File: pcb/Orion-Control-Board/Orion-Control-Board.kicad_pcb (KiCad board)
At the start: 2 copper layers, 35 x 35 mm, 36 parts, among them J1 CORTEX_DEBUG_SWD_UART, J2 STLINK_SWD_JTAG_20POS, J3 USB C 2.0 Female, U1 FT232RL, U2 USBLC6-2SC6, U3 LM66100, U4 LM66100

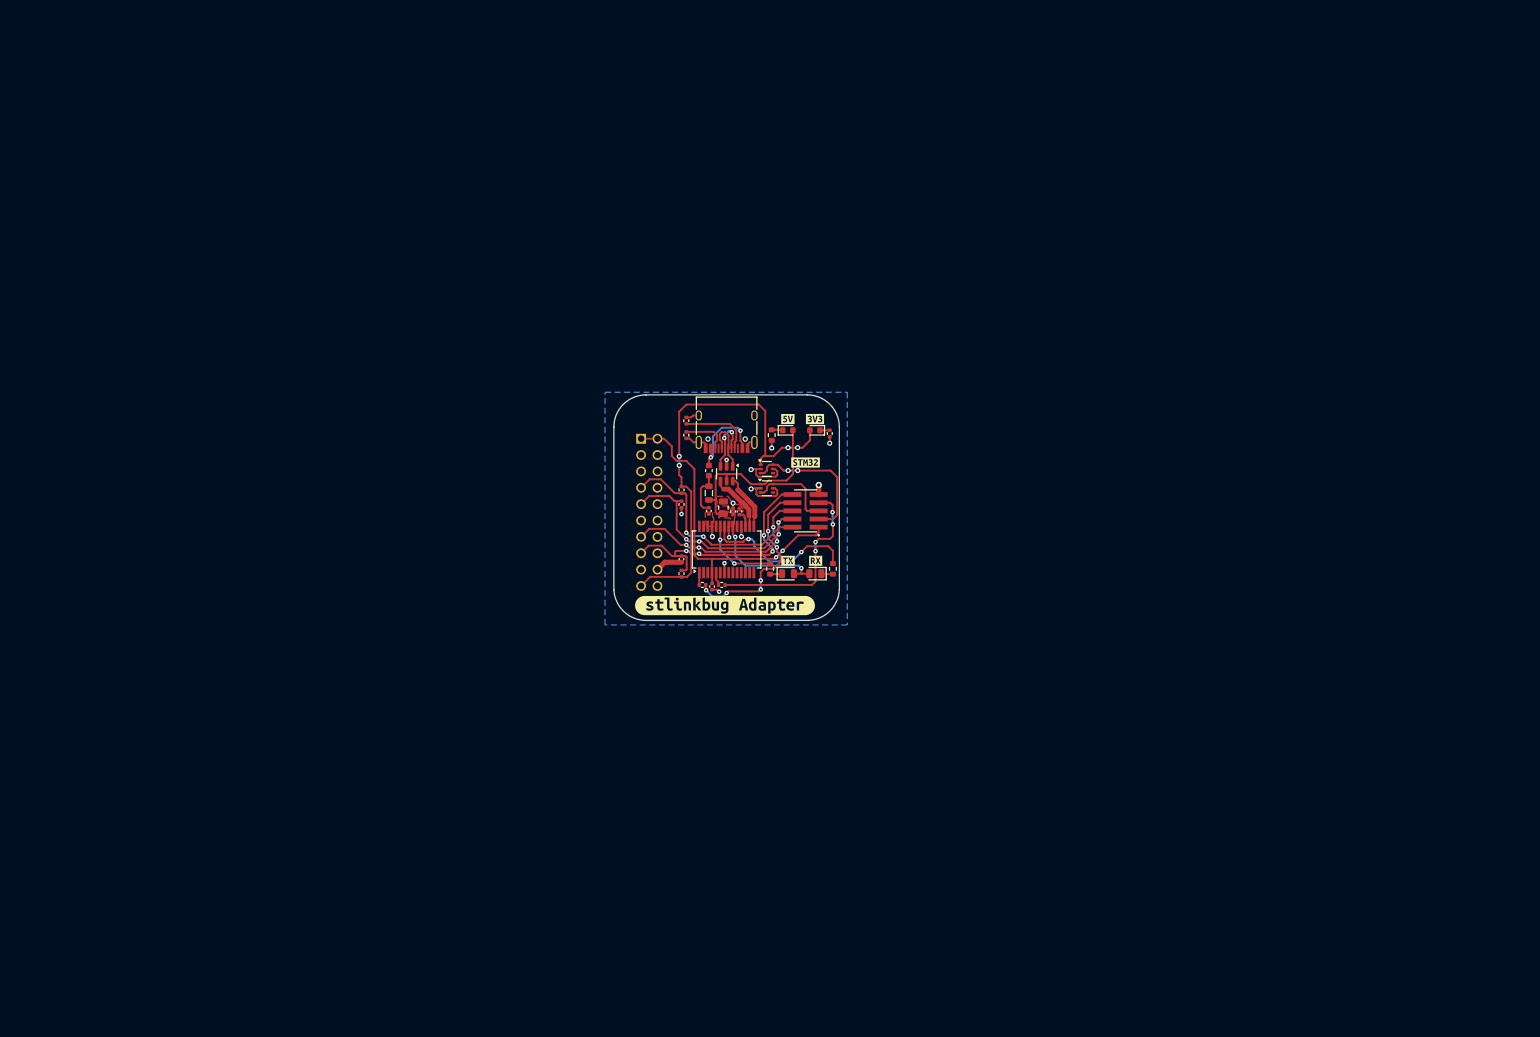
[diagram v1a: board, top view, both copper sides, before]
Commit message: Complete Schematic - Add STM32
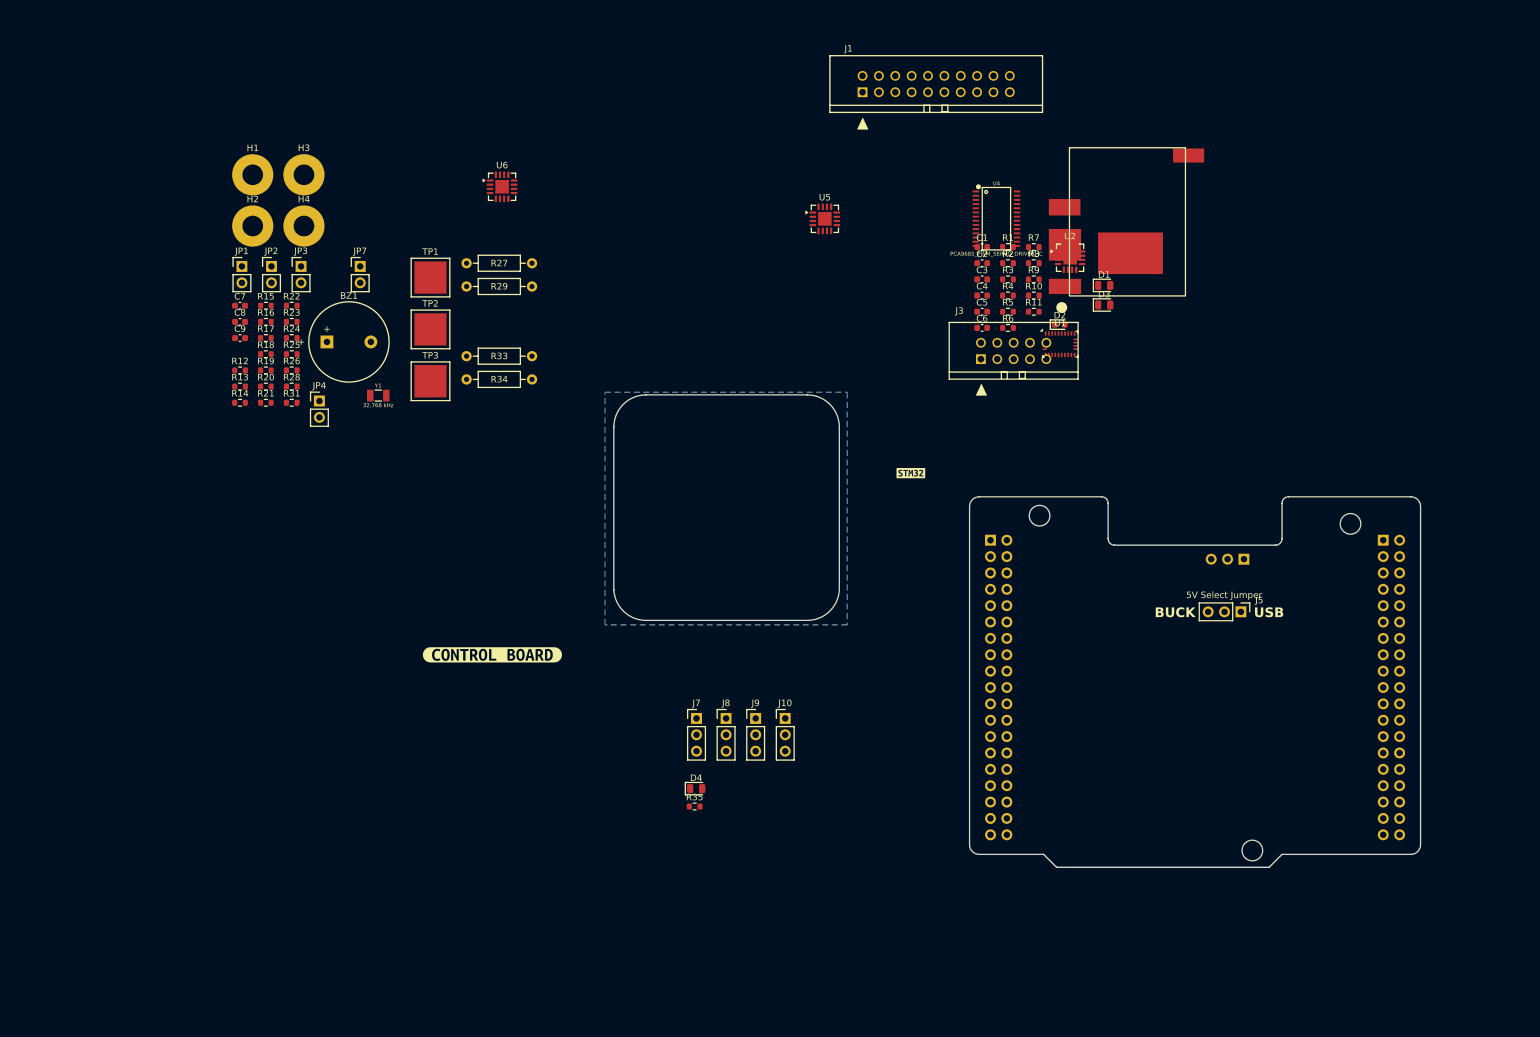
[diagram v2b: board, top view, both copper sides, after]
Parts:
- removed F1: 6V 500mA Fuse, Fuse:Fuse_0603_1608Metric
- removed FB1: 100Ω@100MHz, Inductor_SMD:L_0805_2012Metric
- removed kibuzzard-6742EAFE: G***, kibuzzard-6742EAFE
- removed kibuzzard-6742EB17: G***, kibuzzard-6742EB17
- removed kibuzzard-6742EB21: G***, kibuzzard-6742EB21
- removed kibuzzard-6742EB24: G***, kibuzzard-6742EB24
- removed kibuzzard-67567AD6: G***, kibuzzard-67567AD6
- added BZ1: Buzzer, AA_Custom_Components:Buzzer_Generic_D12.2mm_H6.5mm, F.Cu at (72.5, 76.3)
- added C7: 10uF, Capacitor_SMD:C_0603_1608Metric, F.Cu at (59.0, 70.7)
- added C8: 100nF, Capacitor_SMD:C_0603_1608Metric, F.Cu at (59.0, 73.2)
- added C9: 100nF, Capacitor_SMD:C_0603_1608Metric, F.Cu at (59.0, 75.7)
- added H1: MountingHole, MountingHole:MountingHole_3.2mm_M3_Pad, F.Cu at (61.0, 50.3)
- added H2: MountingHole, MountingHole:MountingHole_3.2mm_M3_Pad, F.Cu at (61.0, 58.3)
- added H3: MountingHole, MountingHole:MountingHole_3.2mm_M3_Pad, F.Cu at (68.9, 50.3)
- added H4: MountingHole, MountingHole:MountingHole_3.2mm_M3_Pad, F.Cu at (68.9, 58.3)
- added H5: MountingHole, MountingHole:MountingHole_3.2mm_M3, F.Cu at (183.1, 103.2)
- added H6: MountingHole, MountingHole:MountingHole_3.2mm_M3, F.Cu at (231.3, 104.5)
- added H7: MountingHole, MountingHole:MountingHole_3.2mm_M3, F.Cu at (216.1, 155.2)
- added J10: POWER, AA_Custom_Components:Jumper_PinHeader_1x03_P2.54mm_Vertical, F.Cu at (143.6, 134.7)
- added J4: 5V Select Socket, Connector_PinSocket_2.54mm:PinSocket_1x03_P2.54mm_Vertical, B.Cu at (214.8, 110.0)
- added J5: 5V Select Jumper, AA_Custom_Components:Jumper_PinHeader_1x03_P2.54mm_Vertical, F.Cu at (214.3, 118.2)
- added J6: NUCLEO64_CN10, Connector_PinSocket_2.54mm:PinSocket_2x19_P2.54mm_Vertical, B.Cu at (236.4, 107.1)
- added J7: I2C 1, AA_Custom_Components:Jumper_PinHeader_1x03_P2.54mm_Vertical, F.Cu at (129.8, 134.7)
- added J8: I2C 3, AA_Custom_Components:Jumper_PinHeader_1x03_P2.54mm_Vertical, F.Cu at (134.4, 134.7)
- added J9: UART, AA_Custom_Components:Jumper_PinHeader_1x03_P2.54mm_Vertical, F.Cu at (139.0, 134.7)
- added JP1: BNO Jumper, AA_Custom_Components:Jumper_PinHeader_1x02_P2.54mm_Vertical, F.Cu at (59.3, 64.6)
- added JP2: V_{Sense1} Jumper, AA_Custom_Components:Jumper_PinHeader_1x02_P2.54mm_Vertical, F.Cu at (63.9, 64.6)
- added JP3: V_{Sense2} Jumper, AA_Custom_Components:Jumper_PinHeader_1x02_P2.54mm_Vertical, F.Cu at (68.5, 64.6)
- added JP4: PCA Jumper, AA_Custom_Components:Jumper_PinHeader_1x02_P2.54mm_Vertical, F.Cu at (71.3, 85.5)
- added JP7: V_{Sense3} Jumper, AA_Custom_Components:Jumper_PinHeader_1x02_P2.54mm_Vertical, F.Cu at (77.6, 64.6)
- added R12: 220, Resistor_SMD:R_0603_1608Metric, F.Cu at (59.0, 80.7)
- added R13: 10k, Resistor_SMD:R_0603_1608Metric, F.Cu at (59.0, 83.2)
- added R14: 10k, Resistor_SMD:R_0603_1608Metric, F.Cu at (59.0, 85.7)
- added R15: 10k, Resistor_SMD:R_0603_1608Metric, F.Cu at (63.0, 70.7)
- added R16: 10k, Resistor_SMD:R_0603_1608Metric, F.Cu at (63.0, 73.2)
- added R17: 10k, Resistor_SMD:R_0603_1608Metric, F.Cu at (63.0, 75.7)
- added R18: 220, Resistor_SMD:R_0603_1608Metric, F.Cu at (63.0, 78.2)
- added R19: 220, Resistor_SMD:R_0603_1608Metric, F.Cu at (63.0, 80.7)
- added R20: 220, Resistor_SMD:R_0603_1608Metric, F.Cu at (63.0, 83.2)
- added R21: 220, Resistor_SMD:R_0603_1608Metric, F.Cu at (63.0, 85.7)
- added R22: 10k, Resistor_SMD:R_0603_1608Metric, F.Cu at (67.0, 70.7)
- added R23: 10k, Resistor_SMD:R_0603_1608Metric, F.Cu at (67.0, 73.2)
- added R24: 10k, Resistor_SMD:R_0603_1608Metric, F.Cu at (67.0, 75.7)
- added R25: 10k, Resistor_SMD:R_0603_1608Metric, F.Cu at (67.0, 78.2)
- added R26: 470, Resistor_SMD:R_0603_1608Metric, F.Cu at (67.0, 80.7)
- added R27: 4.7k, AA_Custom_Components:R_SS_Axial_DIN0207_L6.3mm_D2.5mm_P10.16mm_Horizontal, F.Cu at (94.1, 64.1)
- added R28: 75, Resistor_SMD:R_0603_1608Metric, F.Cu at (67.0, 83.2)
- added R29: 4.7k, AA_Custom_Components:R_SS_Axial_DIN0207_L6.3mm_D2.5mm_P10.16mm_Horizontal, F.Cu at (94.1, 67.7)
- added R31: 75, Resistor_SMD:R_0603_1608Metric, F.Cu at (67.0, 85.7)
- added R33: 4.7k, AA_Custom_Components:R_SS_Axial_DIN0207_L6.3mm_D2.5mm_P10.16mm_Horizontal, F.Cu at (94.1, 78.5)
- added R34: 4.7k, AA_Custom_Components:R_SS_Axial_DIN0207_L6.3mm_D2.5mm_P10.16mm_Horizontal, F.Cu at (94.1, 82.1)
- added R35: 470, Resistor_SMD:R_0603_1608Metric, F.Cu at (129.5, 148.4)
- added TP1: 5V PAD, AA_Custom_Components:TestPoint_Pad_5.0x5.0mm, F.Cu at (88.5, 66.3)
- added TP2: 3.3V PAD, AA_Custom_Components:TestPoint_Pad_5.0x5.0mm, F.Cu at (88.5, 74.3)
- added TP3: GND PAD, AA_Custom_Components:TestPoint_Pad_5.0x5.0mm, F.Cu at (88.5, 82.4)
- added U5: INA3221, Package_DFN_QFN:Texas_RGV0016A_VQFN-16-1EP_4x4mm_P0.65mm_EP2.1x2.1mm, F.Cu at (149.8, 57.2)
- added U6: INA3221, Package_DFN_QFN:Texas_RGV0016A_VQFN-16-1EP_4x4mm_P0.65mm_EP2.1x2.1mm, F.Cu at (99.7, 52.2)
- added Y1: 32.768 kHz, Clocks:CRYSTAL-SMD-3.2X1.5MM, F.Cu at (80.4, 84.6)
- added kibuzzard-693E4A70: G***, kibuzzard-693E4A70, F.Cu at (98.2, 124.8)
- C1, C2: footprint Capacitor_SMD:C_0402_1005Metric -> Capacitor_SMD:C_0603_1608Metric
- C3: value 4.7uF -> 1uF; footprint Capacitor_SMD:C_0805_2012Metric -> Capacitor_SMD:C_0603_1608Metric
- C4: value 10nF -> 100nF; footprint Capacitor_SMD:C_0402_1005Metric -> Capacitor_SMD:C_0603_1608Metric
- C5, C6: value 100nF -> 22pF; footprint Capacitor_SMD:C_0402_1005Metric -> Capacitor_SMD:C_0603_1608Metric
- D1: value 3.3V -> Buck 5V; footprint LED_SMD:LED_0603_1608Metric -> LED_SMD:LED_0805_2012Metric
- D2: value 5V -> STM32 3.3V
- D3: value TX -> DEBUG
- D4: value RX -> USB 5V
- J1: value CORTEX_DEBUG_SWD_UART -> CONN_20_POS_KEYED_SOCKET; footprint AA_Custom_Components:SAMTEC_FTSH-105-XX-X-DV -> AA_Custom_Components:SULLINS_SBH11-PBPC-D10-ST-BK_SOCKET
- J2: value STLINK_SWD_JTAG_20POS -> NUCLEO64_CN7; footprint AA_Custom_Components:SULLINS_SFH11-PBPC-D10-ST-BK -> Connector_PinSocket_2.54mm:PinSocket_2x19_P2.54mm_Vertical
- J3: value USB C 2.0 Female -> JETSON_ORIN_NANO_DEVKIT_GPIO; footprint Connector_USB:USB_C_Receptacle_HRO_TYPE-C-31-M-12 -> AA_Custom_Components:SULLINS_SBH11-PBPC-D05-ST-BK_SOCKET
- R1, R2, R3: value 100k -> 10k; footprint Resistor_SMD:R_0402_1005Metric -> Resistor_SMD:R_0603_1608Metric
- R10, R11: value 100 -> 220; footprint Resistor_SMD:R_0402_1005Metric -> Resistor_SMD:R_0603_1608Metric
- R4: value 100 -> 10k; footprint Resistor_SMD:R_0402_1005Metric -> Resistor_SMD:R_0603_1608Metric
- R5, R6, R7: value 680 -> 220
- R8, R9: value 5k1 -> 220; footprint Resistor_SMD:R_0402_1005Metric -> Resistor_SMD:R_0603_1608Metric
- U1: value FT232RL -> BNO055; footprint Package_SO:SSOP-28_5.3x10.2mm_P0.65mm -> Package_LGA:LGA-28_5.2x3.8mm_P0.5mm
- U2: value USBLC6-2SC6 -> INA3221; footprint Package_TO_SOT_SMD:SOT-23-6 -> Package_DFN_QFN:Texas_RGV0016A_VQFN-16-1EP_4x4mm_P0.65mm_EP2.1x2.1mm
- U3: value LM66100 -> DFR0753 5V BUCK; footprint Package_TO_SOT_SMD:SOT-363_SC-70-6 -> AA_Custom_Components:DFR0753
- U4: value LM66100 -> PCA9685_PWM_SERVO_DRIVER_IC; footprint Package_TO_SOT_SMD:SOT-363_SC-70-6 -> Silicon-Standard:TSSOP-28_4MM
- moved R1 71.7 mm to (178.2, 61.6), turned to 0 degrees
- moved J1 69.3 mm to (167.0, 36.3), turned to 0 degrees
- moved R10 68.3 mm to (182.2, 69.1)
- moved C1 67.3 mm to (174.2, 61.6), turned to 0 degrees
- moved D3 64.4 mm to (193.1, 70.5)
- moved R11 64.4 mm to (182.2, 71.6)
- moved U2 63.0 mm to (187.8, 63.2), turned to 0 degrees
- moved R2 61.7 mm to (178.2, 64.1), turned to 0 degrees
- moved R3 61.5 mm to (178.2, 66.6), turned to 0 degrees
- moved U1 60.8 mm to (186.3, 76.6), turned to 0 degrees
- moved R8 60.2 mm to (182.2, 64.1), turned to 0 degrees
- moved R7 58.9 mm to (182.2, 61.6), turned to 0 degrees
- moved R9 58.2 mm to (182.2, 66.6), turned to 0 degrees
- moved C6 58.0 mm to (174.2, 74.1), turned to 0 degrees
- moved U4 55.0 mm to (176.4, 57.2)
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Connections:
- net TX_{STM32} renamed PWM6
- C1 pad 1: nReset -> GND
- C1 pad 2: GND -> Net-(JP1-A)
- C2 pad 1: GND -> Net-(JP1-A)
- C2 pad 2: Net-(U1-3V3OUT) -> GND
- C3 pad 1: +5V -> Net-(U1-CAP)
- C4 pad 1: Net-(C4-Pad1) -> Net-(JP2-A)
- C5 pad 1: +5V -> Net-(U1-XOUT32)
- C6 pad 1: V_{ref} -> GND
- C6 pad 2: GND -> Net-(U1-XIN32)
- D1 pad 2: +3.3V -> +5V
- D2 pad 2: +5V -> +3.3V
- D3 pad 2: +5V -> LED_DEBUG
- D4 pad 2: +5V -> +USB_5V
- J1 pad 1: V_{ref} -> PWM0
- J1 pad 10: nReset -> PWM9
- J1 pad 2: SWDIO -> PWM1
- J1 pad 3: Net-(J1-3.3V) -> PWM2
- J1 pad 4: SWCLK -> PWM3
- J1 pad 5: Net-(J1-5V) -> PWM4
- J1 pad 6: SWO -> PWM5
- J1 pad 8: RX_{STM32} -> PWM7
- J1 pad 9: GND -> PWM8
- J2 pad 1: V_{ref} -> unconnected-(J2-Pad1)
- J2 pad 10: GND -> unconnected-(J2-Pad10)
- J2 pad 12: GND -> unconnected-(J2-IOREF-Pad12)
- J2 pad 13: SWO -> unconnected-(J2-Pad13)
- J2 pad 14: GND -> unconnected-(J2-RESET-Pad14)
- J2 pad 15: nReset -> unconnected-(J2-Pad15)
- J2 pad 16: GND -> +3.3V
- J2 pad 18: GND -> unconnected-(J2-5V-Pad18)
- J2 pad 19: +3.3V -> GND
- J2 pad 2: V_{ref} -> unconnected-(J2-Pad2)
- J2 pad 3: GND -> unconnected-(J2-Pad3)
- J2 pad 4: GND -> unconnected-(J2-Pad4)
- J2 pad 5: GND -> unconnected-(J2-VDD-Pad5)
- J2 pad 6: GND -> +5V
- J2 pad 7: SWDIO -> unconnected-(J2-BOOT0-Pad7)
- J2 pad 9: SWCLK -> unconnected-(J2-Pad9)
- R1 pad 1: +3.3V -> Net-(U2-PV)
- R1 pad 2: nReset -> Net-(JP2-A)
- R10 pad 1: Net-(U1-TXD) -> Net-(U4-CH5)
- R10 pad 2: RX_{STM32} -> PWM5
- R11 pad 1: Net-(U1-RXD) -> Net-(U4-CH6)
- R2 pad 1: +3.3V -> Net-(U2-CRITICAL)
- R2 pad 2: SWDIO -> Net-(JP2-A)
- R3 pad 1: SWCLK -> Net-(U2-WARNING)
- R3 pad 2: GND -> Net-(JP2-A)
- R4 pad 1: Net-(D1-K) -> Net-(U2-TC)
- R4 pad 2: GND -> Net-(JP2-A)
- R5 pad 1: Net-(D2-K) -> Net-(U4-CH0)
- R5 pad 2: GND -> PWM0
- R6 pad 1: Net-(D3-K) -> Net-(U4-CH1)
- R6 pad 2: /TXLED -> PWM1
- R7 pad 1: Net-(D4-K) -> Net-(U4-CH2)
- R7 pad 2: /RXLED -> PWM2
- R8 pad 1: Net-(J3-CC2) -> Net-(U4-CH3)
- R8 pad 2: GND -> PWM3
- R9 pad 1: Net-(J3-CC1) -> Net-(U4-CH4)
- R9 pad 2: GND -> PWM4
- U1 pad 1: Net-(U1-TXD) -> unconnected-(U1-PIN1-Pad1)
- U1 pad 11: unconnected-(U1-CTS-Pad11) -> +3.3V
- U1 pad 15: D+ -> unconnected-(U1-PIN15-Pad15)
- U1 pad 16: D- -> unconnected-(U1-PIN16-Pad16)
- U1 pad 17: Net-(U1-3V3OUT) -> GND
- U1 pad 19: unconnected-(U1-~{RESET}-Pad19) -> SCL_{3}
- U1 pad 2: unconnected-(U1-DTR-Pad2) -> GND
- U1 pad 20: +5V -> SDA_{3}
- U1 pad 21: GND -> unconnected-(U1-PIN21-Pad21)
- U1 pad 22: /RXLED -> unconnected-(U1-PIN22-Pad22)
- U1 pad 23: /TXLED -> unconnected-(U1-PIN23-Pad23)
- U1 pad 24: (no net) -> unconnected-(U1-PIN24-Pad24)
- U1 pad 26: GND -> Net-(U1-XOUT32)
- U1 pad 27: unconnected-(U1-OSCI-Pad27) -> Net-(U1-XIN32)
- U1 pad 28: unconnected-(U1-OSCO-Pad28) -> Net-(JP1-A)
- U1 pad 3: unconnected-(U1-RTS-Pad3) -> Net-(JP1-A)
- U1 pad 4: V_{ref} -> +3.3V
- U1 pad 5: Net-(U1-RXD) -> GND
- U1 pad 6: unconnected-(U1-RI-Pad6) -> GND
- U1 pad 7: GND -> unconnected-(U1-PIN7-Pad7)
- U1 pad 8: (no net) -> unconnected-(U1-PIN8-Pad8)
- U1 pad 9: unconnected-(U1-DCR-Pad9) -> Net-(U1-CAP)
- U2 pad 1: /CONN_D+ -> unconnected-(U2-IN-3-Pad1)
- U2 pad 2: GND -> unconnected-(U2-IN+3-Pad2)
- U2 pad 3: /CONN_D- -> GND
- U2 pad 4: D- -> Net-(JP2-A)
- U2 pad 5: +5V -> +3.3V
- U2 pad 6: D+ -> SCL_{2}
- U3 pad 1: +3.3V -> 2S_BATT_FRONT_CELL2
- U3 pad 3: Net-(J1-3.3V) -> +5V
- U3 pad 5: GND -> unconnected-(U3-MOUNT-Pad5)
- U4 pad 1: +5V -> GND
- U4 pad 3: Net-(J1-5V) -> GND
- U4 pad 4: unconnected-(U4-NC-Pad4) -> GND
- U4 pad 6: Net-(J1-5V) -> Net-(U4-CH0)
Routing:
- net +3.3V: track 67.4 -> 0.00 mm, vias 4 -> 0
- net V_{ref}: track 50.4 -> 0.00 mm, vias 2 -> 0
- net +5V: track 48.3 -> 0.00 mm, vias 2 -> 0
- net GND: track 41.7 -> 0.00 mm, vias 13 -> 0
- net nReset: track 39.6 -> 0.00 mm, vias 4 -> 0
- net SWCLK: track 33.7 -> 0.00 mm, vias 4 -> 0
- net SWDIO: track 32.8 -> 0.00 mm, vias 2 -> 0
- net SWO: track 31.1 -> 0.00 mm, vias 4 -> 0
- net PWM6: track 30.6 -> 0.00 mm, vias 4 -> 0
- net RX_{STM32}: track 29.2 -> 0.00 mm, vias 6 -> 0
- net /RXLED: track 24.3 -> 0.00 mm, vias 2 -> 0
- net Net-(J1-3.3V): track 22.5 -> 0.00 mm, vias 2 -> 0
- net Net-(F1-Pad1): track 14.1 -> 0.00 mm, vias 2 -> 0
- net Net-(J1-5V): track 13.4 -> 0.00 mm
- net /TXLED: track 12.3 -> 0.00 mm, vias 2 -> 0
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- removed copper zone on F.Cu, net +5V
- removed copper zone on F.Cu, net GND
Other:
- board size 35 x 35 mm -> 125.2 x 73.3 mm
- board text added: "5V Select Jumper"
- board text added: "BUCK"
- board text added: "USB"

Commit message: Update JLCPCB rules
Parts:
- JP2: value V_{Sense1} Jumper -> VSense1 Jumper
- JP3: value V_{Sense2} Jumper -> VSense2 Jumper
- JP7: value V_{Sense3} Jumper -> VSense3 Jumper
- moved kibuzzard-6742FB76 134.0 mm to (49.2, 26.0)
- moved J8 132.9 mm to (243.0, 58.1)
- moved J9 132.9 mm to (247.6, 58.1)
- moved D4 132.9 mm to (238.4, 69.0)
- moved J10 132.9 mm to (252.2, 58.1)
- moved J7 132.9 mm to (238.4, 58.1)
- moved R35 132.9 mm to (238.1, 71.8)
- moved J1 117.0 mm to (131.4, 147.7)
- moved kibuzzard-693E4A70 105.0 mm to (49.6, 31.8)
- moved U3 69.2 mm to (136.8, 115.9), turned to 180 degrees
- moved H5 66.3 mm to (116.8, 105.0)
- moved H6 66.3 mm to (165.0, 106.3)
- moved H7 66.3 mm to (149.8, 157.0)
- moved J2 66.3 mm to (109.2, 108.8)
- moved J6 66.3 mm to (170.1, 108.8)
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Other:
- board size 125.2 x 73.3 mm -> 74.5 x 67.5 mm

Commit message: Update symbols
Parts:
- J10, J5, J7, J8, J9: footprint AA_Custom_Components:Jumper_PinHeader_1x03_P2.54mm_Vertical -> digikey-footprints:PinHeader_1x3_P2.54_Drill1.1mm
- J4: footprint Connector_PinSocket_2.54mm:PinSocket_1x03_P2.54mm_Vertical -> digikey-footprints:PinHeader_1x3_P2.54_Drill1.1mm
- U2, U5, U6: footprint Package_DFN_QFN:Texas_RGV0016A_VQFN-16-1EP_4x4mm_P0.65mm_EP2.1x2.1mm -> AA_Custom_Components:Texas_RGV0016A_VQFN-16-1EP_4x4mm_P0.65mm_EP2.1x2.1mm_ThermalVias
- U4: footprint Silicon-Standard:TSSOP-28_4MM -> AA_Custom_Components:TSSOP-28_4MM
- turned J4 to 180 degrees
- turned J5 to 180 degrees
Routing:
- net GND: track 0.00 -> 20.1 mm, vias 0 -> 8
- net Net-(J4-Pad3): track 0.00 -> 3.88 mm
- net Net-(J4-Pad2): track 0.00 -> 3.88 mm
- net Net-(J4-Pad1): track 0.00 -> 3.88 mm
